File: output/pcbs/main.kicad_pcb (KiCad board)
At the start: 2 copper layers, 110.3 x 90.1 mm, 84 parts, among them Q1 AO3400A, SW1 CPG1316S01D02_reversible, SW10 CPG1316S01D02_reversible, SW11 CPG1316S01D02_reversible, SW12 CPG1316S01D02_reversible, SW13 CPG1316S01D02_reversible, SW14 CPG1316S01D02_reversible, SW15 CPG1316S01D02_reversible, SW16 CPG1316S01D02_reversible, SW17 CPG1316S01D02_reversible, SW18 CPG1316S01D02_reversible, SW2 CPG1316S01D02_reversible, SW3 CPG1316S01D02_reversible, SW4 CPG1316S01D02_reversible, SW5 CPG1316S01D02_reversible, SW6 CPG1316S01D02_reversible, SW7 CPG1316S01D02_reversible, SW8 CPG1316S01D02_reversible, SW9 CPG1316S01D02_reversible

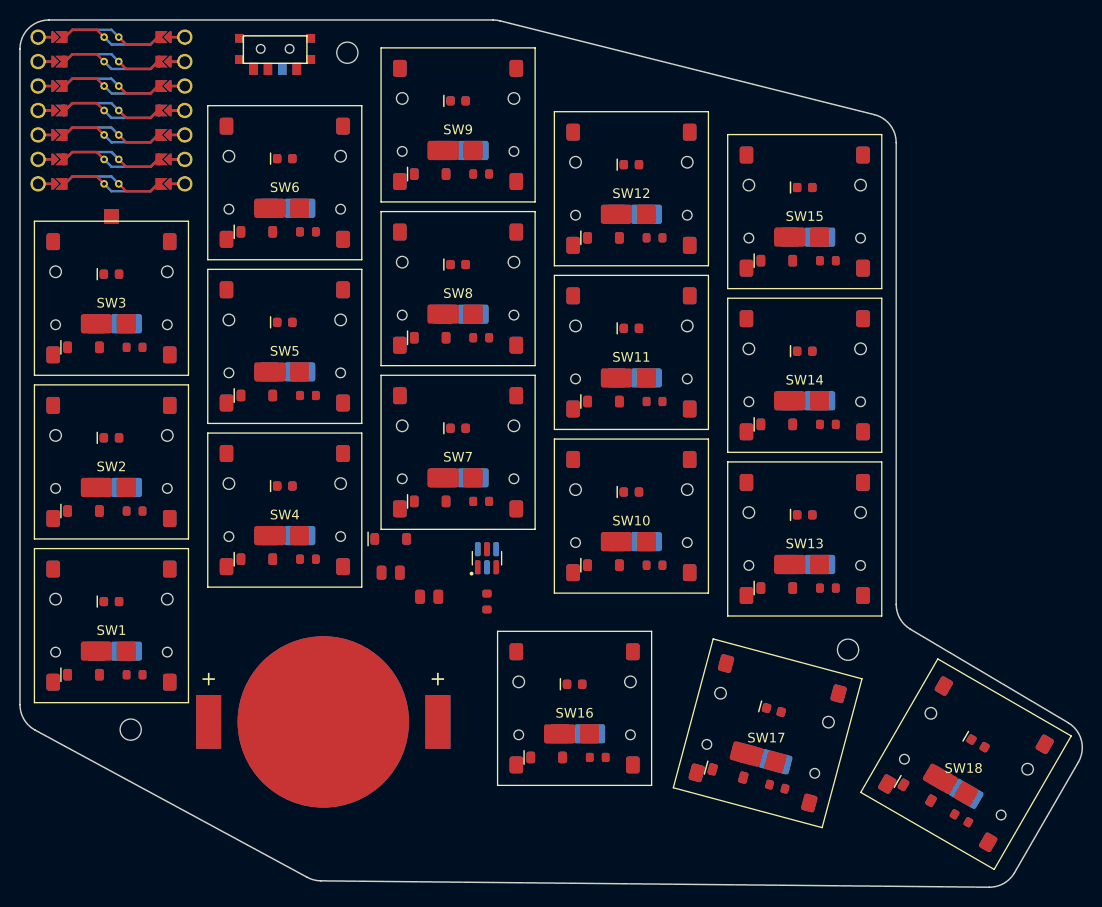
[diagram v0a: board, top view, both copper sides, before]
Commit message: Re-route the board with the diode next to the LED
Co-Authored-By: Claude Sonnet 5.5 <noreply@anthropic.com>
Claude-Session: https://claude.ai/code/session_0165D9fBjcdWGjdLPuN9BjoD
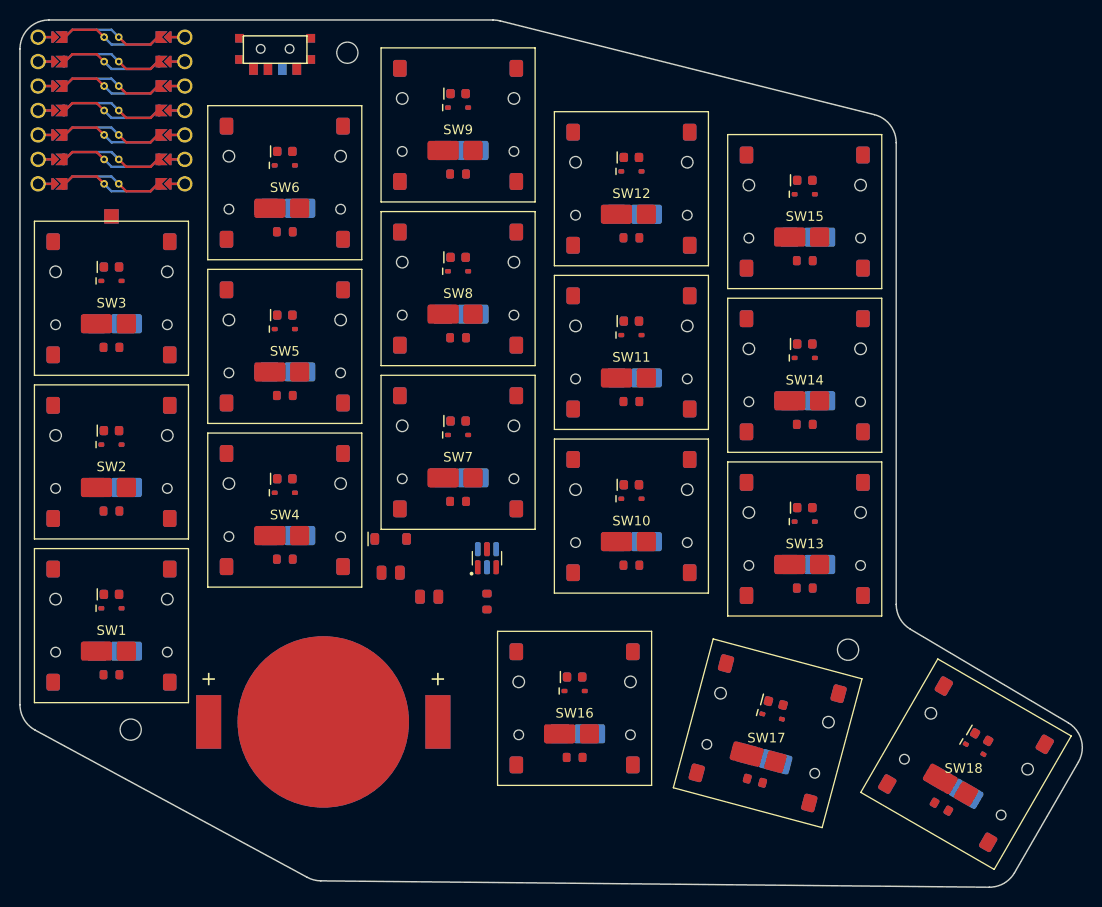
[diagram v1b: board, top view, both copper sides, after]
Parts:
- D1, D10, D11, D12, D13, D14, D15, D16, D17, D18, D2, D3, D4, D5, D6, D7, D8, D9: value 1N4148W -> 1N4148WS; footprint ucw:REV_SOD123 -> ucw:REV_SOD323
- moved D18 7.48 mm to (89.7, 12.8)
- moved D17 7.48 mm to (68.6, 9.44)
- moved D14 7.48 mm to (72.0, -27.8)
- moved D13 7.48 mm to (72.0, -10.8)
- moved D11 7.48 mm to (54.0, -30.2)
- moved D5 7.48 mm to (18.0, -30.8)
- moved D15 7.48 mm to (72.0, -44.8)
- moved D10 7.48 mm to (54.0, -13.2)
- moved D2 7.48 mm to (0.00, -18.8)
- moved D3 7.48 mm to (0.00, -35.8)
- moved D4 7.48 mm to (18.0, -13.8)
- moved D6 7.48 mm to (18.0, -47.8)
- moved D7 7.48 mm to (36.0, -19.8)
- moved D1 7.48 mm to (0.00, -1.80)
- moved D16 7.48 mm to (48.1, 6.79)
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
